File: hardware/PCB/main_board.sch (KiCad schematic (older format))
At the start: 3 parts

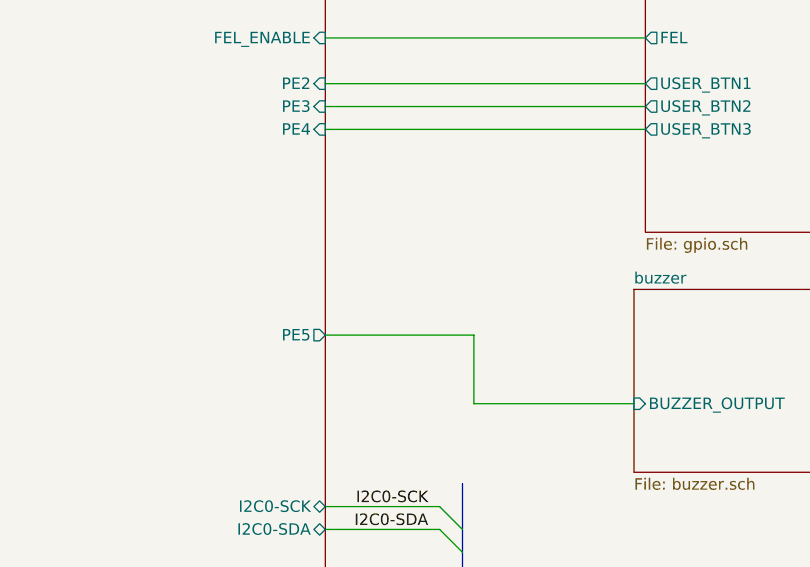
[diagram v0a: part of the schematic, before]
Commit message: pcb: update for selective buzzer input,
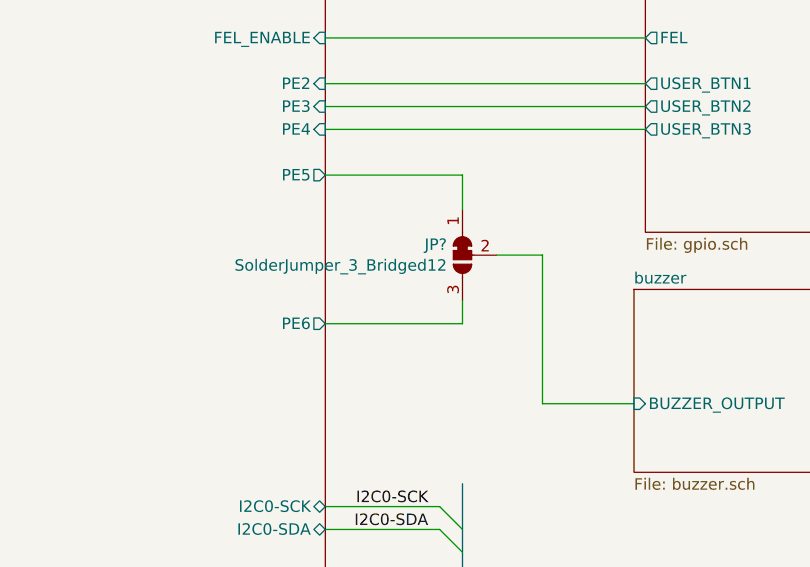
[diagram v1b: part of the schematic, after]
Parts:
- added JP?: SolderJumper_3_Bridged12, symbol Jumper:SolderJumper_3_Bridged12
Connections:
- net buzzer/BUZZER_OUTPUT: now also JP?.2 (C)
- new net licheepi_nano/PE5: JP?.1 (A)
- new net licheepi_nano/PE6: JP?.3 (B)
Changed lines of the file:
@@
 $EndSheet
 Wire Wire Line
-	7050 3900 7700 3900
-Wire Wire Line
-	7700 3900 7700 4200
-Wire Wire Line
-	7700 4200 8400 4200
+	8000 4200 8400 4200
 $Sheet
 S 4800 2400 2250 3200
@@
 F10 "PE3" I R 7050 2900 50
 F11 "PE4" I R 7050 3000 50
-F12 "PE5" O R 7050 3900 50
+F12 "PE5" O R 7050 3200 50
 F13 "UART0_TX" I L 4800 3450 50
 F14 "UART0_RX" I L 4800 3550 50
@@
 F23 "SPI0_CLK" I R 7050 5300 50
 F24 "SPI0_MISO" I R 7050 5400 50
+F25 "PE6" O R 7050 3850 50
 $EndSheet
 $Comp
@@
 Text Label 7500 5400 2    50   ~ 0
 SPI0_MISO
-Wire Bus Line
-	7650 4550 7650 6150
-Wire Bus Line
-	4150 2300 4150 3050
-Wire Bus Line
-	3550 2300 3550 3050
 Wire Wire Line
 	3950 3350 4200 3350
@@
 	0    -1   -1   0
 $EndComp
+$Comp
+L Jumper:SolderJumper_3_Bridged12 JP?
+U 1 1 5E9B36BC
+P 7650 3550
+F 0 "JP?" V 7604 3618 50  0000 L CNN
+F 1 "SolderJumper_3_Bridged12" V 7695 3618 50  0000 L CNN
+F 2 "" H 7650 3550 50  0001 C CNN
+F 3 "~" H 7650 3550 50  0001 C CNN
+	1    7650 3550
+	0    -1   1    0
+$EndComp
+Wire Wire Line
+	7800 3550 8000 3550
+Wire Wire Line
+	8000 3550 8000 4200
+Wire Wire Line
+	7050 3850 7650 3850
+Wire Wire Line
+	7650 3850 7650 3750
+Wire Wire Line
+	7050 3200 7650 3200
+Wire Wire Line
+	7650 3200 7650 3350
+Wire Bus Line
+	3550 2300 3550 3050
+Wire Bus Line
+	4150 2300 4150 3050
+Wire Bus Line
+	7650 4550 7650 6150
 $EndSCHEMATC
